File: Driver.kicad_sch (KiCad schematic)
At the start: 4 parts

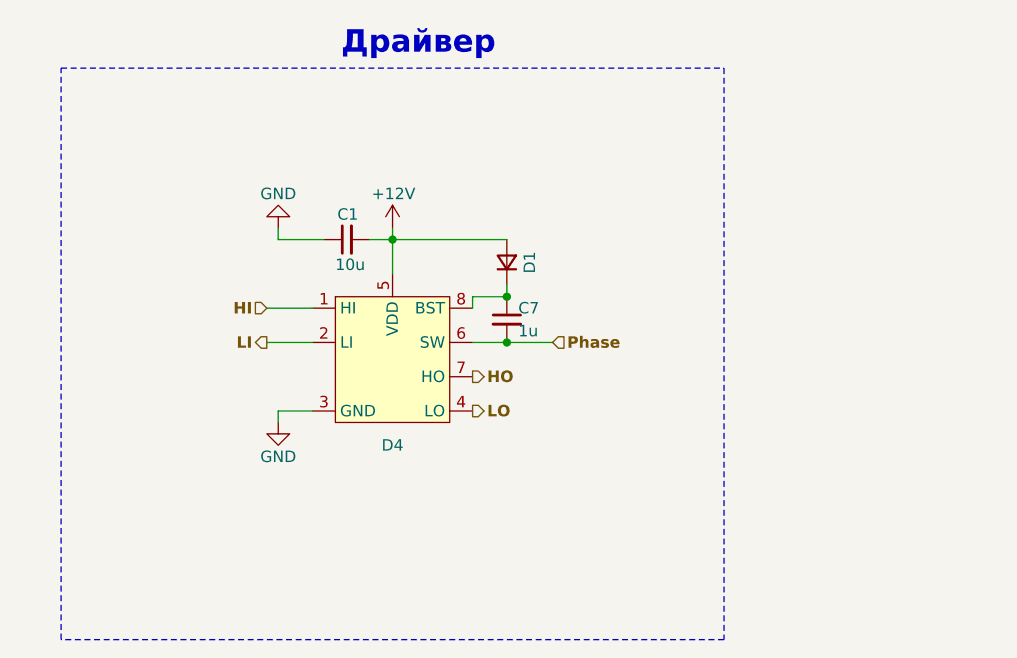
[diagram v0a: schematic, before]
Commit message: §3, §5, §6 схема: NetTie SW, ветвь выключения на позицию, C_gs, снабберы, RC на HI/LI
Driver.kicad_sch: SW драйвера — своя цепь через NetTie NT1–NT3; на HO и LO
R_on 0.82 Ом ∥ (D_off PMEG4010BEA + R_off 0 Ом), R106–R117, D30–D35; на HI/LI
R 0 Ом + C 100 пФ DNP (R118–R123, C118–C123).
Phase_A.kicad_sch: R_g 2.7 Ом 0805 -> 1 Ом 0603; C_gs 4.7 нФ DNP C100–C111;
снабберы LS и HS DNP (C112–C117, R100–R105).
ERC — 9 ошибок (база), netlist сверен по цепям: +57 компонентов, прочие связи
без изменений. ТЗ: Р3 — термистор остаётся на узле, Р10 — VDC→J6 можно
перекладывать.

Co-Authored-By: Claude Opus 5.5 <noreply@anthropic.com>
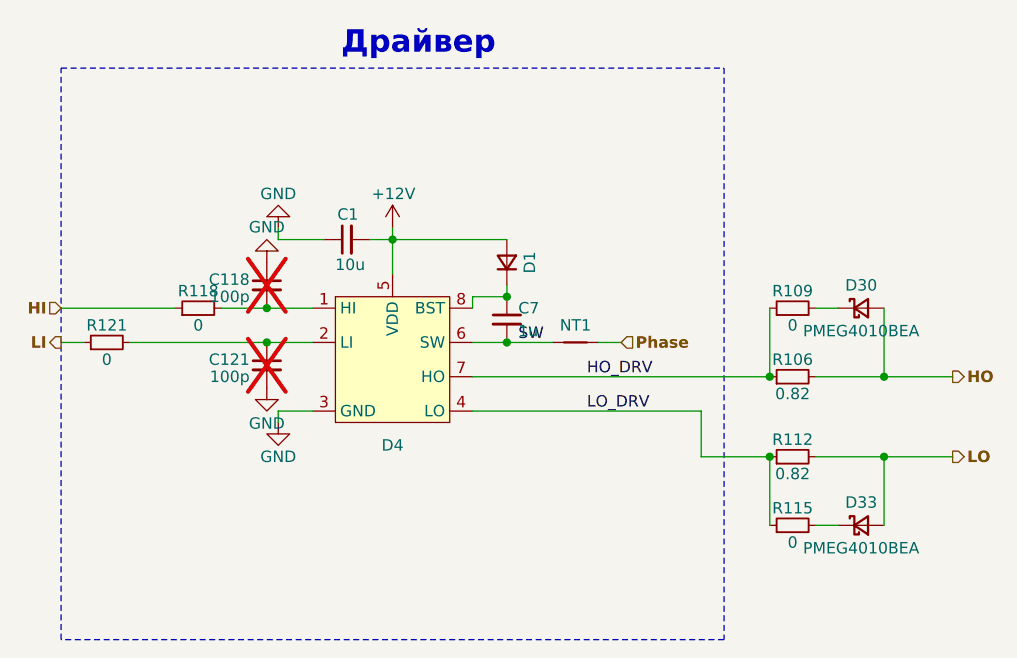
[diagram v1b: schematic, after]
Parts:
- added C118, C121: 100p, Capacitor_SMD:C_0603_1608Metric_Pad1.08x0.95mm_HandSolder, symbol Device:C_Small
- added D30, D33: PMEG4010BEA, Diode_SMD:D_SOD-323_HandSoldering, symbol Device:D_Schottky_Small
- added NT1: NetTie_2, NetTie:NetTie-2_SMD_Pad0.5mm, symbol Device:NetTie_2
- added R106, R112: 0.82, Resistor_SMD:R_0805_2012Metric_Pad1.20x1.40mm_HandSolder, symbol Device:R_Small
- added R109, R115, R118, R121: 0, Resistor_SMD:R_0603_1608Metric_Pad0.98x0.95mm_HandSolder, symbol Device:R_Small
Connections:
- net GND: now also C118.1, C121.2
- net HI: now also R118.1; no longer D4.1 (HI)
- net HO: now also D30.2 (A), R106.2; no longer D4.7 (HO)
- net LI: now also R121.1; no longer D4.2 (LI)
- net LO: now also D33.2 (A), R112.2; no longer D4.4 (LO)
- net Phase: now also NT1.2; no longer C7.2, D4.6 (SW)
- new net: C118.2, D4.1 (HI), R118.2
- new net: C121.1, D4.2 (LI), R121.2
- new net: D30.1 (K), R109.2
- new net: D33.1 (K), R115.2
- new net HO_DRV: D4.7 (HO), R106.1, R109.1
- new net LO_DRV: D4.4 (LO), R112.1, R115.1
- new net SW: C7.2, D4.6 (SW), NT1.1

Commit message: Схема, второй заход: ветвь выключения без R_off, керамика §4 (Р14, Р15)
R_off (R109–R111, R115–R117) убраны — D_off прямо от X к выводу драйвера;
R_on — 0603, D_off — стандартный SOD-323. Керамика петли C124–C135,
1 мкФ 100 В 1206, по 4 на фазу. ERC — 9 ошибок (база), netlist сверен.

Co-Authored-By: Claude Opus 5.5 <noreply@anthropic.com>
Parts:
- removed R109, R115: 0, Resistor_SMD:R_0603_1608Metric_Pad0.98x0.95mm_HandSolder, symbol Device:R_Small
- D30, D33: footprint Diode_SMD:D_SOD-323_HandSoldering -> Diode_SMD:D_SOD-323
- R106, R112: footprint Resistor_SMD:R_0805_2012Metric_Pad1.20x1.40mm_HandSolder -> Resistor_SMD:R_0603_1608Metric_Pad0.98x0.95mm_HandSolder
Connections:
- net HO_DRV: now also D30.1 (K)
- net LO_DRV: now also D33.1 (K)
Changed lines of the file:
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@@
+		)
+	)
+	(wire
+		(pts
+			(xy 184.15 96.52) (xy 189.23 96.52)
+		)
+		(stroke
+			(width 0)
+			(type default)
+		)
+	)
+	(wire
+		(pts
+			(xy 184.15 120.65) (xy 189.23 120.65)
+		)
+		(stroke
+			(width 0)
+			(type default)
 		)
 	)
@@
 			)
 		)
-		(property "Footprint" "Resistor_SMD:R_0805_2012Metric_Pad1.20x1.40mm_HandSolder"
+		(property "Footprint" "Resistor_SMD:R_0603_1608Metric_Pad0.98x0.95mm_HandSolder"
 			(at 186.69 104.14 0)
 			(hide yes)
@@
 			(width 0)
 			(type default)
-		)
-	)
-	(symbol
-		(lib_id "Device:R_Small")
-		(at 186.69 96.52 90)
-		(unit 1)
-		(body_style 1)
-		(exclude_from_sim no)
-		(in_bom yes)
-		(on_board yes)
-		(in_pos_files yes)
-		(dnp no)
-		(property "Reference" "R109"
-			(at 186.69 94.615 90)
-			(show_name no)
-			(do_not_autoplace no)
-			(effects
-				(font
-					(size 1.27 1.27)
-				)
-			)
-		)
-		(property "Value" "0"
-			(at 186.69 98.425 90)
-			(show_name no)
-			(do_not_autoplace no)
-			(effects
-				(font
-					(size 1.27 1.27)
-				)
-			)
-		)
-		(property "Footprint" "Resistor_SMD:R_0603_1608Metric_Pad0.98x0.95mm_HandSolder"
-			(at 186.69 96.52 0)
-			(hide yes)
-			(show_name no)
-			(do_not_autoplace no)
-			(effects
-				(font
-					(size 1.27 1.27)
-				)
-			)
-		)
-		(property "Datasheet" ""
-			(at 186.69 96.52 0)
-			(hide yes)
-			(show_name no)
-			(do_not_autoplace no)
-			(effects
-				(font
-					(size 1.27 1.27)
-				)
-			)
-		)
-		(property "Description" ""
-			(at 186.69 96.52 0)
-			(hide yes)
-			(show_name no)
-			(do_not_autoplace no)
-			(effects
-				(font
-					(size 1.27 1.27)
-				)
-			)
-		)
-		(property "Description P/N" "Resistor SMD 1%"
-			(at 186.69 96.52 0)
-			(hide yes)
-			(show_name no)
-			(do_not_autoplace no)
-			(effects
-				(font
-					(size 1.27 1.27)
-				)
-			)
-		)
-		(pin "1"
-		)
-		(pin "2"
-		)
-		(instances
-			(project "Power"
-				(path "/7ff38f8b-11c9-43a1-8b76-b5e8c8de18e0/a8d734bd-b043-4b16-b834-36ede11366f7"
-					(reference "R109")
-					(unit 1)
-				)
-				(path "/7ff38f8b-11c9-43a1-8b76-b5e8c8de18e0/47ea5ea6-75b2-417d-becc-0c7b63ba572f"
-					(reference "R110")
-					(unit 1)
-				)
-				(path "/7ff38f8b-11c9-43a1-8b76-b5e8c8de18e0/f6f48504-43ae-4516-9932-88fd69aadde3"
-					(reference "R111")
-					(unit 1)
-				)
-			)
 		)
 	)
@@
 			)
 		)
-		(property "Footprint" "Diode_SMD:D_SOD-323_HandSoldering"
+		(property "Footprint" "Diode_SMD:D_SOD-323"
 			(at 194.31 96.52 0)
 			(hide yes)
@@
 			)
 		)
-		(property "Footprint" "Resistor_SMD:R_0805_2012Metric_Pad1.20x1.40mm_HandSolder"
+		(property "Footprint" "Resistor_SMD:R_0603_1608Metric_Pad0.98x0.95mm_HandSolder"
 			(at 186.69 113.03 0)
 			(hide yes)
@@
 			(width 0)
 			(type default)
-		)
-	)
-	(symbol
-		(lib_id "Device:R_Small")
-		(at 186.69 120.65 90)
-		(unit 1)
-		(body_style 1)
-		(exclude_from_sim no)
-		(in_bom yes)
-		(on_board yes)
-		(in_pos_files yes)
-		(dnp no)
-		(property "Reference" "R115"
-			(at 186.69 118.745 90)
-			(show_name no)
-			(do_not_autoplace no)
-			(effects
-				(font
-					(size 1.27 1.27)
-				)
-			)
-		)
-		(property "Value" "0"
-			(at 186.69 122.555 90)
-			(show_name no)
-			(do_not_autoplace no)
-			(effects
-				(font
-					(size 1.27 1.27)
-				)
-			)
-		)
-		(property "Footprint" "Resistor_SMD:R_0603_1608Metric_Pad0.98x0.95mm_HandSolder"
-			(at 186.69 120.65 0)
-			(hide yes)
-			(show_name no)
-			(do_not_autoplace no)
-			(effects
-				(font
-					(size 1.27 1.27)
-				)
-			)
-		)
-		(property "Datasheet" ""
-			(at 186.69 120.65 0)
-			(hide yes)
-			(show_name no)
-			(do_not_autoplace no)
-			(effects
-				(font
-					(size 1.27 1.27)
-				)
-			)
-		)
-		(property "Description" ""
-			(at 186.69 120.65 0)
-			(hide yes)
-			(show_name no)
-			(do_not_autoplace no)
-			(effects
-				(font
-					(size 1.27 1.27)
-				)
-			)
-		)
-		(property "Description P/N" "Resistor SMD 1%"
-			(at 186.69 120.65 0)
-			(hide yes)
-			(show_name no)
-			(do_not_autoplace no)
-			(effects
-				(font
-					(size 1.27 1.27)
-				)
-			)
-		)
-		(pin "1"
-		)
-		(pin "2"
-		)
-		(instances
-			(project "Power"
-				(path "/7ff38f8b-11c9-43a1-8b76-b5e8c8de18e0/a8d734bd-b043-4b16-b834-36ede11366f7"
-					(reference "R115")
-					(unit 1)
-				)
-				(path "/7ff38f8b-11c9-43a1-8b76-b5e8c8de18e0/47ea5ea6-75b2-417d-becc-0c7b63ba572f"
-					(reference "R116")
-					(unit 1)
-				)
-				(path "/7ff38f8b-11c9-43a1-8b76-b5e8c8de18e0/f6f48504-43ae-4516-9932-88fd69aadde3"
-					(reference "R117")
-					(unit 1)
-				)
-			)
 		)
 	)
@@
 			)
 		)
-		(property "Footprint" "Diode_SMD:D_SOD-323_HandSoldering"
+		(property "Footprint" "Diode_SMD:D_SOD-323"
 			(at 194.31 120.65 0)
 			(hide yes)

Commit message: Д1, Д2: C_gs C100–C111 — 10 нФ C0G, ставятся; D_off D30–D35 — DNP (схема и плата); Д3 снят решением владельца
Co-Authored-By: Claude Opus 5.5 <noreply@anthropic.com>
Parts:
- D30, D33: now not fitted
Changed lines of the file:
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@@
 		(on_board yes)
 		(in_pos_files yes)
-		(dnp no)
+		(dnp yes)
 		(property "Reference" "D30"
 			(at 194.31 93.98 0)
@@
 		(on_board yes)
 		(in_pos_files yes)
-		(dnp no)
+		(dnp yes)
 		(property "Reference" "D33"
 			(at 194.31 118.11 0)

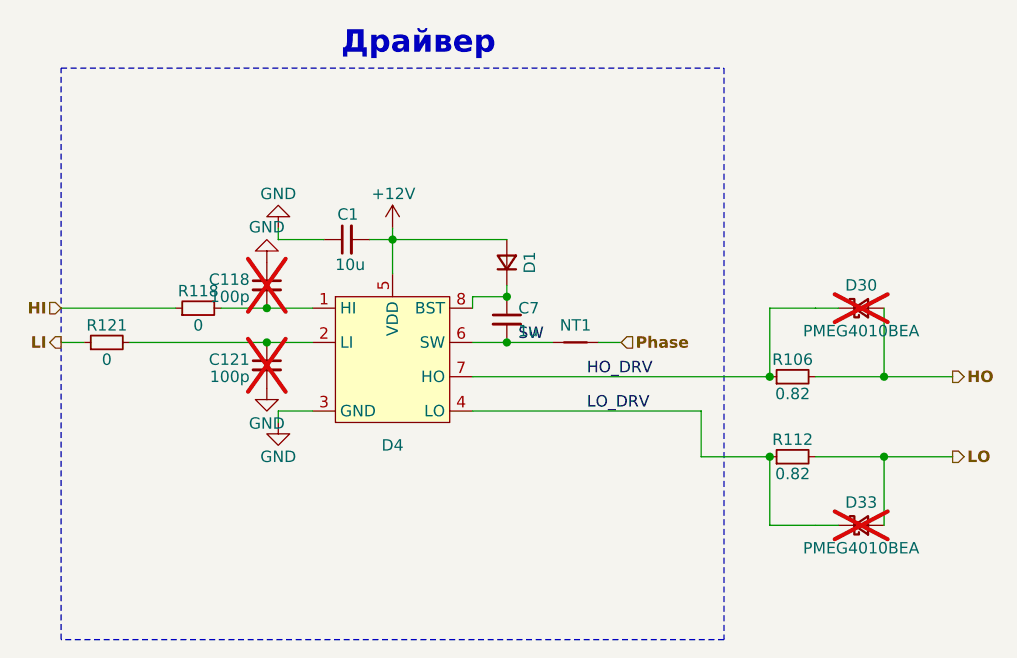
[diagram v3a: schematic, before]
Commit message: Правки владельца: R8 (0603) последовательно в DAC_1_MCU на B.Cu у TP1, трасса DAC перезаведена по B.Cu; порядок листов и Power.kicad_pro пересохранены KiCad
Co-Authored-By: Claude Opus 5.5 <noreply@anthropic.com>
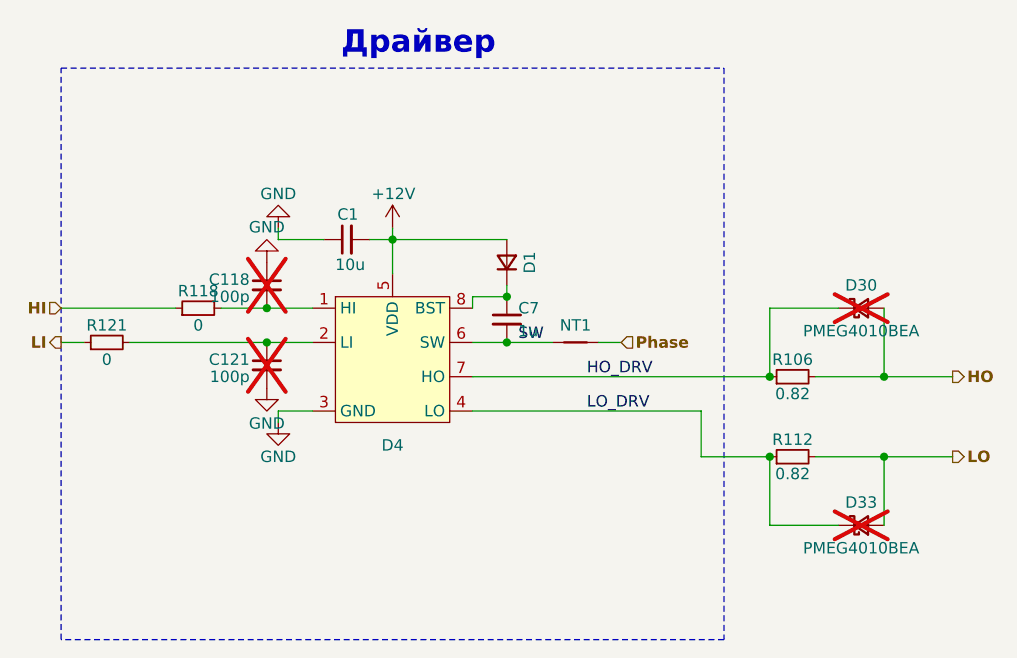
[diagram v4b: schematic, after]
